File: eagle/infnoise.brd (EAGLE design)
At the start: 31.8 x 13.4 mm, 25 parts, among them SW1 NS5B1G385DFT2G, SW2 NS5B1G385DFT2G, U1 FT240XQ, X1 USBSMT-MALE

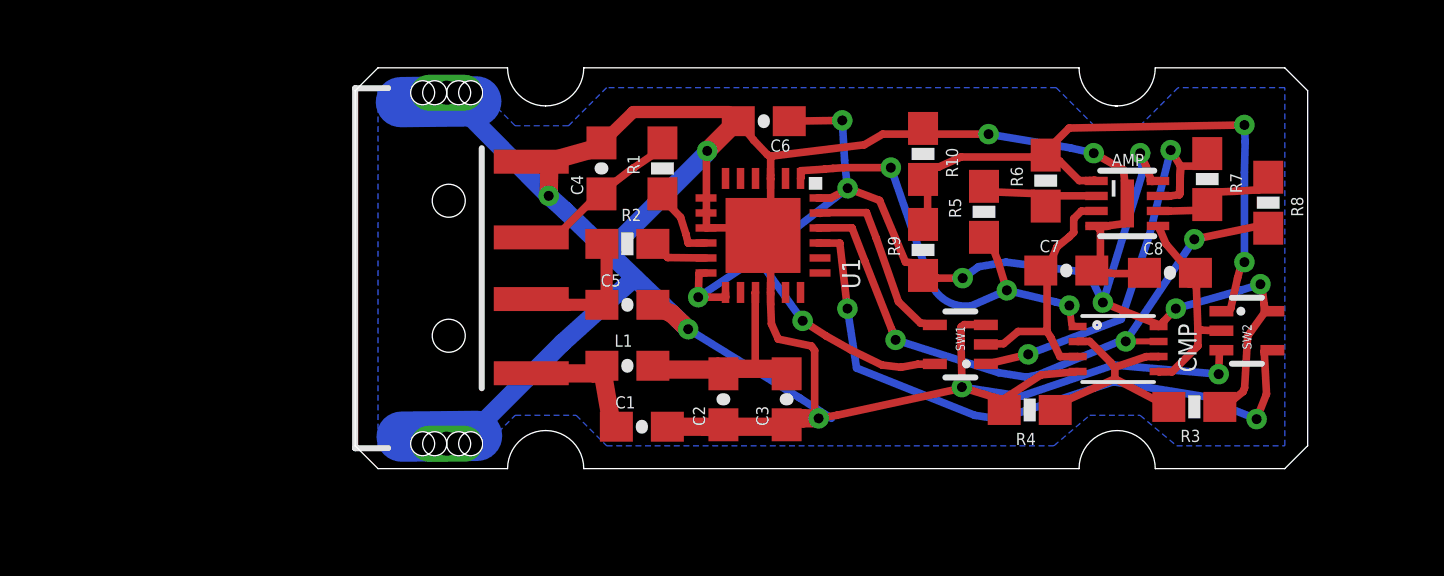
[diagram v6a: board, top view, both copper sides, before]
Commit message: Updates to board based on fixes to breadboard
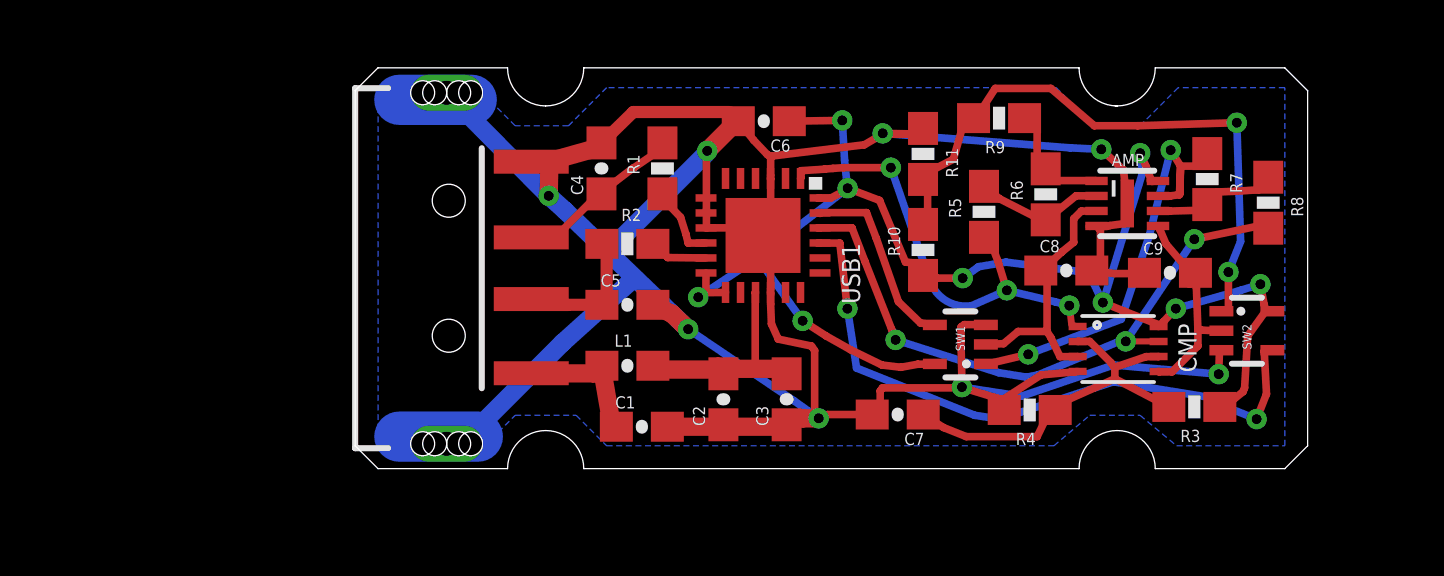
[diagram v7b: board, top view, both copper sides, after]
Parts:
- added C9: 100pF, infnoise:0603-CAP
- added R11: 810K, infnoise:0603-RES
- C7: value 100pF -> 100nF
- R10: value 8.2K -> 10K
- R9: value 8.2K -> 1K
- SW1, SW2: value NS5B1G385DFT2G -> MC74VHC1G66DFT1G
- moved C7 7.39 mm to (18.1, 1.80), turned to 180 degrees
- moved R9 5.07 mm to (21.5, 11.7), turned to 180 degrees
- moved C8 3.46 mm to (23.7, 6.60)
- moved R10 3.20 mm to (18.9, 7.29), turned to 90 degrees
- moved R6 0.46 mm to (23.0, 9.14)
- renumbered U1 to USB1
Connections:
- new net N$1: AMP.1, R6.2, R9.1
- net A: now also C8.1; no longer C7.1
- net AMP1OUT: now also R11.2; no longer AMP.1, R6.2
- net B: now also C9.2; no longer C8.2
- net GND: now also C8.2, C9.1, R11.1; no longer C8.1, R10.1
- net VCC33: now also R10.1; no longer R9.1
- net VREF: now also C7.1
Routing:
- net VREF: track 7.91 -> 13.0 mm
- net N$1: track 0.00 -> 4.18 mm
- net GND: track 110.7 -> 114.3 mm
- net AMP1OUT: track 23.5 -> 22.4 mm
- net VCC33: track 51.3 -> 50.6 mm
